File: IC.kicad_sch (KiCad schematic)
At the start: 24 parts, among them IC1 BTS722204ESAXUMA1

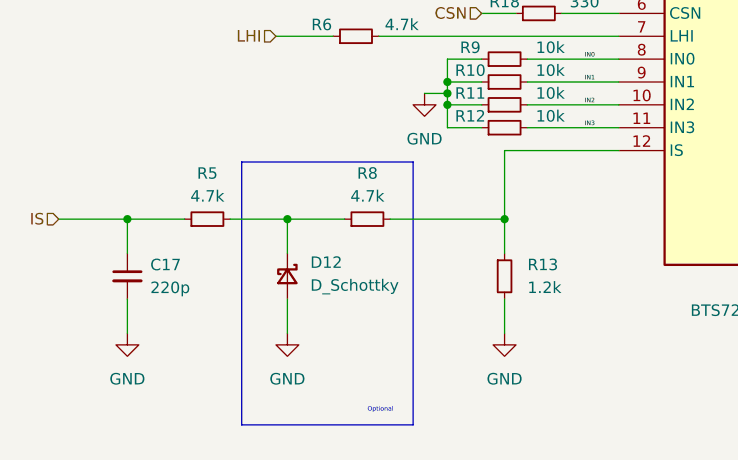
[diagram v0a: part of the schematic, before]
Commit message: Minor changes
Added battery zone on the f.cu
Easier connector soldering (additional pads)
Changed 3.3V layer
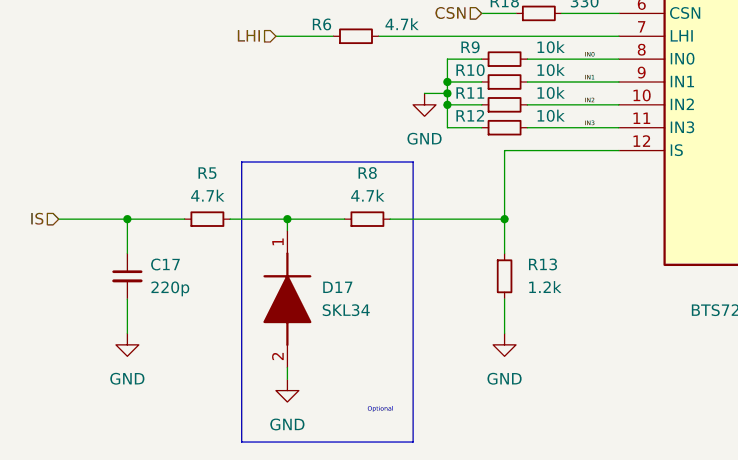
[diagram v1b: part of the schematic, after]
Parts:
- removed D12: D_Schottky, Diode_SMD:D_SMA, symbol Device:D_Schottky_Small
- added D17: SKL34, SODFL3718X140N, symbol SKL34:SKL34
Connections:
- net GND: now also D17.2 (A)
- net at R5.2, R8.1: now also D17.1 (K)
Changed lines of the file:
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@@
 	)
 	(junction
-		(at 99.06 113.03)
-		(diameter 0)
-		(color 0 0 0 0)
-	)
-	(junction
 		(at 171.45 102.87)
 		(diameter 0)
@@
 		(color 0 0 0 0)
 	)
+	(junction
+		(at 99.06 113.03)
+		(diameter 0)
+		(color 0 0 0 0)
+	)
 	(wire
 		(pts
@@
 	(wire
 		(pts
-			(xy 99.06 113.03) (xy 105.41 113.03)
-		)
-		(stroke
-			(width 0)
-			(type default)
-		)
-	)
-	(wire
-		(pts
 			(xy 120.65 82.55) (xy 124.46 82.55)
 		)
@@
 	(wire
 		(pts
-			(xy 99.06 121.92) (xy 99.06 125.73)
+			(xy 184.15 113.03) (xy 184.15 116.84)
 		)
 		(stroke
@@
 	(wire
 		(pts
-			(xy 184.15 113.03) (xy 184.15 116.84)
+			(xy 171.45 105.41) (xy 190.5 105.41)
 		)
 		(stroke
@@
 	(wire
 		(pts
-			(xy 99.06 113.03) (xy 99.06 116.84)
+			(xy 147.32 66.04) (xy 147.32 69.85)
 		)
 		(stroke
@@
 	(wire
 		(pts
-			(xy 171.45 105.41) (xy 190.5 105.41)
+			(xy 116.84 95.25) (xy 116.84 97.79)
 		)
 		(stroke
@@
 	(wire
 		(pts
-			(xy 147.32 66.04) (xy 147.32 69.85)
+			(xy 132.08 54.61) (xy 132.08 57.15)
 		)
 		(stroke
@@
 	(wire
 		(pts
-			(xy 116.84 95.25) (xy 116.84 97.79)
+			(xy 177.8 77.47) (xy 200.66 77.47)
 		)
 		(stroke
@@
 	(wire
 		(pts
-			(xy 132.08 54.61) (xy 132.08 57.15)
+			(xy 99.06 129.54) (xy 99.06 130.81)
 		)
 		(stroke
@@
 	(wire
 		(pts
-			(xy 177.8 77.47) (xy 200.66 77.47)
+			(xy 81.28 113.03) (xy 81.28 116.84)
 		)
 		(stroke
@@
 	(wire
 		(pts
-			(xy 81.28 113.03) (xy 81.28 116.84)
+			(xy 129.54 85.09) (xy 135.89 85.09)
 		)
 		(stroke
@@
 	(wire
 		(pts
-			(xy 129.54 85.09) (xy 135.89 85.09)
+			(xy 99.06 113.03) (xy 105.41 113.03)
 		)
 		(stroke
@@
 	(wire
 		(pts
+			(xy 99.06 114.3) (xy 99.06 113.03)
+		)
+		(stroke
+			(width 0)
+			(type default)
+		)
+	)
+	(wire
+		(pts
 			(xy 81.28 113.03) (xy 87.63 113.03)
 		)
@@
 	(rectangle
 		(start 93.98 106.68)
-		(end 113.03 135.89)
+		(end 113.03 137.795)
 		(stroke
 			(width 0)
@@
 	)
 	(symbol
+		(lib_id "SKL34:SKL34")
+		(at 99.06 114.3 270)
+		(unit 1)
+		(exclude_from_sim no)
+		(in_bom yes)
+		(on_board yes)
+		(dnp no)
+		(fields_autoplaced yes)
+		(property "Reference" "D17"
+			(at 102.87 120.6499 90)
+			(effects
+				(font
+					(size 1.27 1.27)
+				)
+				(justify left)
+			)
+		)
+		(property "Value" "SKL34"
+			(at 102.87 123.1899 90)
+			(effects
+				(font
+					(size 1.27 1.27)
+				)
+				(justify left)
+			)
+		)
+		(property "Footprint" "SODFL3718X140N"
+			(at 1.6 125.73 0)
+			(effects
+				(font
+					(size 1.27 1.27)
+				)
+				(justify left top)
+				(hide yes)
+			)
+		)
+		(property "Datasheet" "http://diotec.com/tl_files/diotec/files/pdf/datasheets/skl32"
+			(at -98.4 125.73 0)
+			(effects
+				(font
+					(size 1.27 1.27)
+				)
+				(justify left top)
+				(hide yes)
+			)
+		)
+		(property "Description" "SMD Schottky Barrier Rectifier Diodes"
+			(at 99.06 114.3 0)
+			(effects
+				(font
+					(size 1.27 1.27)
+				)
+				(hide yes)
+			)
+		)
+		(property "Height" "1.4"
+			(at -298.4 125.73 0)
+			(effects
+				(font
+					(size 1.27 1.27)
+				)
+				(justify left top)
+				(hide yes)
+			)
+		)
+		(property "Mouser Part Number" "637-SKL34"
+			(at -398.4 125.73 0)
+			(effects
+				(font
+					(size 1.27 1.27)
+				)
+				(justify left top)
+				(hide yes)
+			)
+		)
+		(property "Mouser Price/Stock" "https://www.mouser.co.uk/ProductDetail/Diotec-Semiconductor/SKL34?qs=OlC7AqGiEDlypja3QtYFUQ%3D%3D"
+			(at -498.4 125.73 0)
+			(effects
+				(font
+					(size 1.27 1.27)
+				)
+				(justify left top)
+				(hide yes)
+			)
+		)
+		(property "Manufacturer_Name" "Diotec"
+			(at -598.4 125.73 0)
+			(effects
+				(font
+					(size 1.27 1.27)
+				)
+				(justify left top)
+				(hide yes)
+			)
+		)
+		(property "Manufacturer_Part_Number" "SKL34"
+			(at -698.4 125.73 0)
+			(effects
+				(font
+					(size 1.27 1.27)
+				)
+				(justify left top)
+				(hide yes)
+			)
+		)
+		(pin "2"
+		)
+		(pin "1"
+		)
+		(instances
+			(project ""
+				(path "/b652b05a-4e3d-4ad1-b032-18886abe7d45/fd7d6fe4-610a-44c2-815e-0a8f21ae1980/69056856-febd-417e-9880-84d5995904f1"
+					(reference "D16")
+					(unit 1)
+				)
+				(path "/b652b05a-4e3d-4ad1-b032-18886abe7d45/fd7d6fe4-610a-44c2-815e-0a8f21ae1980/92c363b3-7436-43ed-9ade-94e88aef3fa4"
+					(reference "D19")
+					(unit 1)
+				)
+				(path "/b652b05a-4e3d-4ad1-b032-18886abe7d45/fd7d6fe4-610a-44c2-815e-0a8f21ae1980/9c9ff1be-4d96-4366-a088-7fe7ef755fb3"
+					(reference "D17")
+					(unit 1)
+				)
+				(path "/b652b05a-4e3d-4ad1-b032-18886abe7d45/fd7d6fe4-610a-44c2-815e-0a8f21ae1980/d1ea8f7f-291f-487b-9cb1-80f6251ddf1c"
+					(reference "D18")
+					(unit 1)
+				)
+			)
+		)
+	)
+	(symbol
 		(lib_id "Device:R_Small")
 		(at 127 90.17 90)
@@
 	(symbol
 		(lib_id "power:GND")
-		(at 99.06 125.73 0)
+		(at 99.06 130.81 0)
 		(unit 1)
 		(exclude_from_sim no)
@@
 		(fields_autoplaced yes)
 		(property "Reference" "#PWR058"
-			(at 99.06 132.08 0)
+			(at 99.06 137.16 0)
 			(effects
 				(font
@@
 		)
 		(property "Value" "GND"
-			(at 99.06 130.81 0)
+			(at 99.06 135.89 0)
 			(effects
 				(font
@@
 		)
 		(property "Footprint" ""
-			(at 99.06 125.73 0)
+			(at 99.06 130.81 0)
 			(effects
 				(font
@@
 		)
 		(property "Datasheet" ""
-			(at 99.06 125.73 0)
+			(at 99.06 130.81 0)
 			(effects
 				(font
@@
 		)
 		(property "Description" ""
-			(at 99.06 125.73 0)
+			(at 99.06 130.81 0)
 			(effects
 				(font
@@
 					(unit 1)
 				)
-			)
-		)
-	)
-	(symbol
-		(lib_id "Device:D_Schottky_Small")
-		(at 99.06 119.38 270)
-		(unit 1)
-		(exclude_from_sim no)
-		(in_bom yes)
-		(on_board yes)
-		(dnp no)
-		(fields_autoplaced yes)
-		(property "Reference" "D12"
-			(at 101.6 117.856 90)
-			(effects
-				(font
-					(size 1.27 1.27)
-				)
-				(justify left)
-			)
-		)
-		(property "Value" "D_Schottky"
-			(at 101.6 120.396 90)
-			(effects
-				(font
-					(size 1.27 1.27)
-				)
-				(justify left)
-			)
-		)
-		(property "Footprint" "Diode_SMD:D_SMA"
-			(at 99.06 119.38 90)
-			(effects
-				(font
-					(size 1.27 1.27)
-				)
-				(hide yes)
-			)
-		)
-		(property "Datasheet" "https://www.mouser.pl/ProductDetail/Taiwan-Semiconductor/SS34ALH?qs=A6eO%252BMLsxmQip%2FrgNup6RA%3D%3D"
-			(at 99.06 119.38 90)
-			(effects
-				(font
-					(size 1.27 1.27)
-				)
-				(hide yes)
-			)
-		)
-		(property "Description" ""
-			(at 99.06 119.38 0)
-			(effects
-				(font
-					(size 1.27 1.27)
-				)
-				(hide yes)
-			)
-		)
-		(property "m" "SS34ALH"
-			(at 99.06 119.38 90)
-			(effects
-				(font
-					(size 1.27 1.27)
-				)
-				(hide yes)
-			)
-		)
-		(pin "1"
-		)
-		(pin "2"
-		)
-		(instances
-			(project "PUTM_EV_PDMv2_2024"
-				(path "/b652b05a-4e3d-4ad1-b032-18886abe7d45/fd7d6fe4-610a-44c2-815e-0a8f21ae1980/69056856-febd-417e-9880-84d5995904f1"
-					(reference "D12")
-					(unit 1)
-				)
-				(path "/b652b05a-4e3d-4ad1-b032-18886abe7d45/fd7d6fe4-610a-44c2-815e-0a8f21ae1980/92c363b3-7436-43ed-9ade-94e88aef3fa4"
-					(reference "D15")
-					(unit 1)
-				)
-				(path "/b652b05a-4e3d-4ad1-b032-18886abe7d45/fd7d6fe4-610a-44c2-815e-0a8f21ae1980/9c9ff1be-4d96-4366-a088-7fe7ef755fb3"
-					(reference "D13")
-					(unit 1)
-				)
-				(path "/b652b05a-4e3d-4ad1-b032-18886abe7d45/fd7d6fe4-610a-44c2-815e-0a8f21ae1980/d1ea8f7f-291f-487b-9cb1-80f6251ddf1c"
-					(reference "D14")
-					(unit 1)
-				)

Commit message: Production
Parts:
- renumbered D17 to D16
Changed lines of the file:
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@@
 		(dnp no)
 		(fields_autoplaced yes)
-		(property "Reference" "D17"
+		(property "Reference" "D16"
 			(at 102.87 120.6499 90)
 			(effects
@@
 		(exclude_from_sim no)
 		(in_bom yes)
-		(on_board no)
+		(on_board yes)
 		(dnp no)
 		(fields_autoplaced yes)
@@
 		(exclude_from_sim no)
 		(in_bom yes)
-		(on_board no)
+		(on_board yes)
 		(dnp no)
 		(fields_autoplaced yes)
@@
 		(exclude_from_sim no)
 		(in_bom yes)
-		(on_board no)
+		(on_board yes)
 		(dnp no)
 		(fields_autoplaced yes)
@@
 		(exclude_from_sim no)
 		(in_bom yes)
-		(on_board no)
+		(on_board yes)
 		(dnp no)
 		(fields_autoplaced yes)

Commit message: Minor fixes
added USBc tvs
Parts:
- C21, C22, C23, C24: footprint Capacitor_SMD:C_0603_1608Metric_Pad1.08x0.95mm_HandSolder -> Capacitor_SMD:C_0805_2012Metric
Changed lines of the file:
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@@
 			)
 		)
-		(property "Footprint" "Capacitor_SMD:C_0603_1608Metric_Pad1.08x0.95mm_HandSolder"
+		(property "Footprint" "Capacitor_SMD:C_0805_2012Metric"
 			(at 177.8 82.55 0)
 			(effects
@@
 			)
 		)
-		(property "Footprint" "Capacitor_SMD:C_0603_1608Metric_Pad1.08x0.95mm_HandSolder"
+		(property "Footprint" "Capacitor_SMD:C_0805_2012Metric"
 			(at 186.69 100.33 0)
 			(effects
@@
 			)
 		)
-		(property "Footprint" "Capacitor_SMD:C_0603_1608Metric_Pad1.08x0.95mm_HandSolder"
+		(property "Footprint" "Capacitor_SMD:C_0805_2012Metric"
 			(at 190.5 109.22 0)
 			(effects
@@
 			)
 		)
-		(property "Footprint" "Capacitor_SMD:C_0603_1608Metric_Pad1.08x0.95mm_HandSolder"
+		(property "Footprint" "Capacitor_SMD:C_0805_2012Metric"
 			(at 181.61 91.44 0)
 			(effects
